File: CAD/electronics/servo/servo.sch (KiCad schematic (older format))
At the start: 16 parts, among them J1 Front ultrasound, J10 Servo7, J11 Start trigger, J2 Rear ultrasound, J3 Servo0, J4 Servo2, J5 Servo4, J6 Servo6, J7 Servo1, J8 Servo3, J9 Servo5, U1 PCF8574

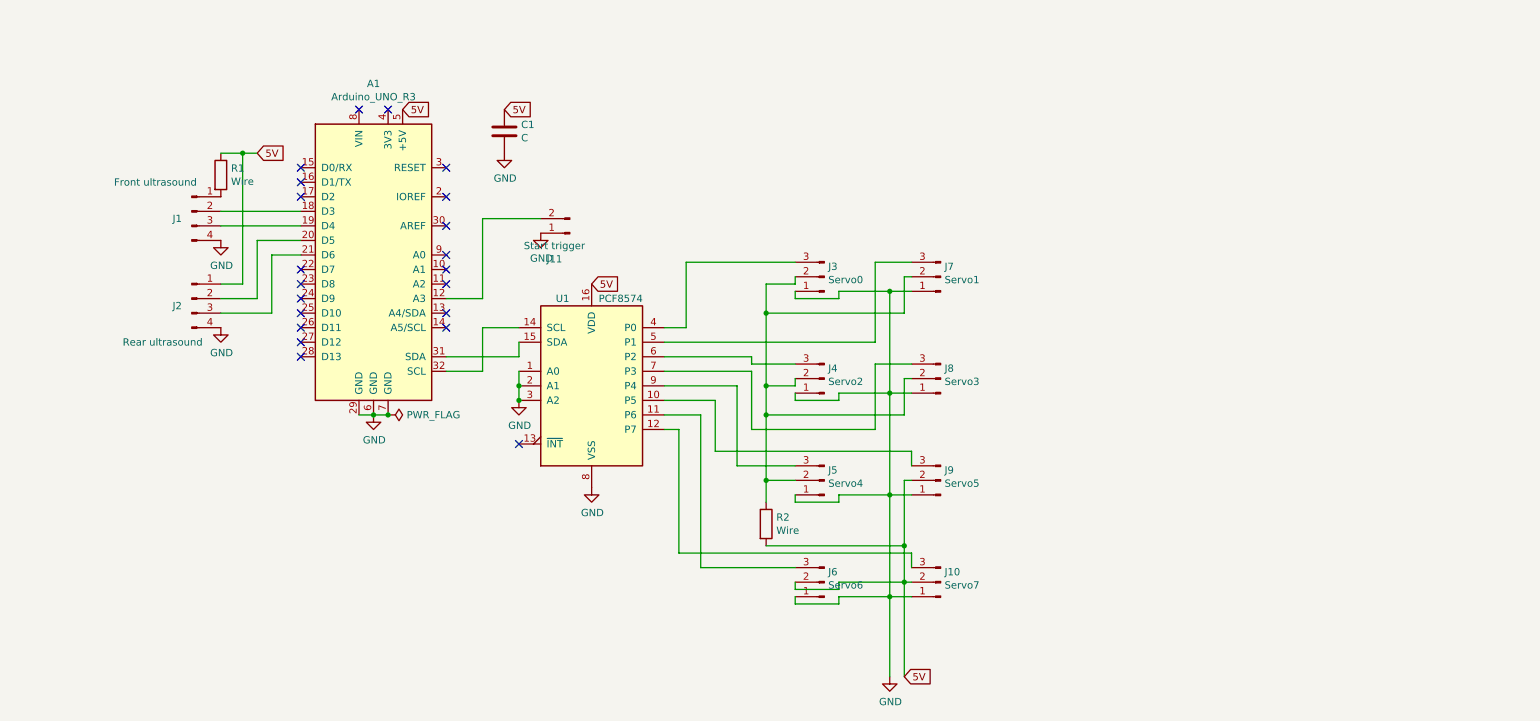
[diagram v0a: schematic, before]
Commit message: Add servo board CAD design.
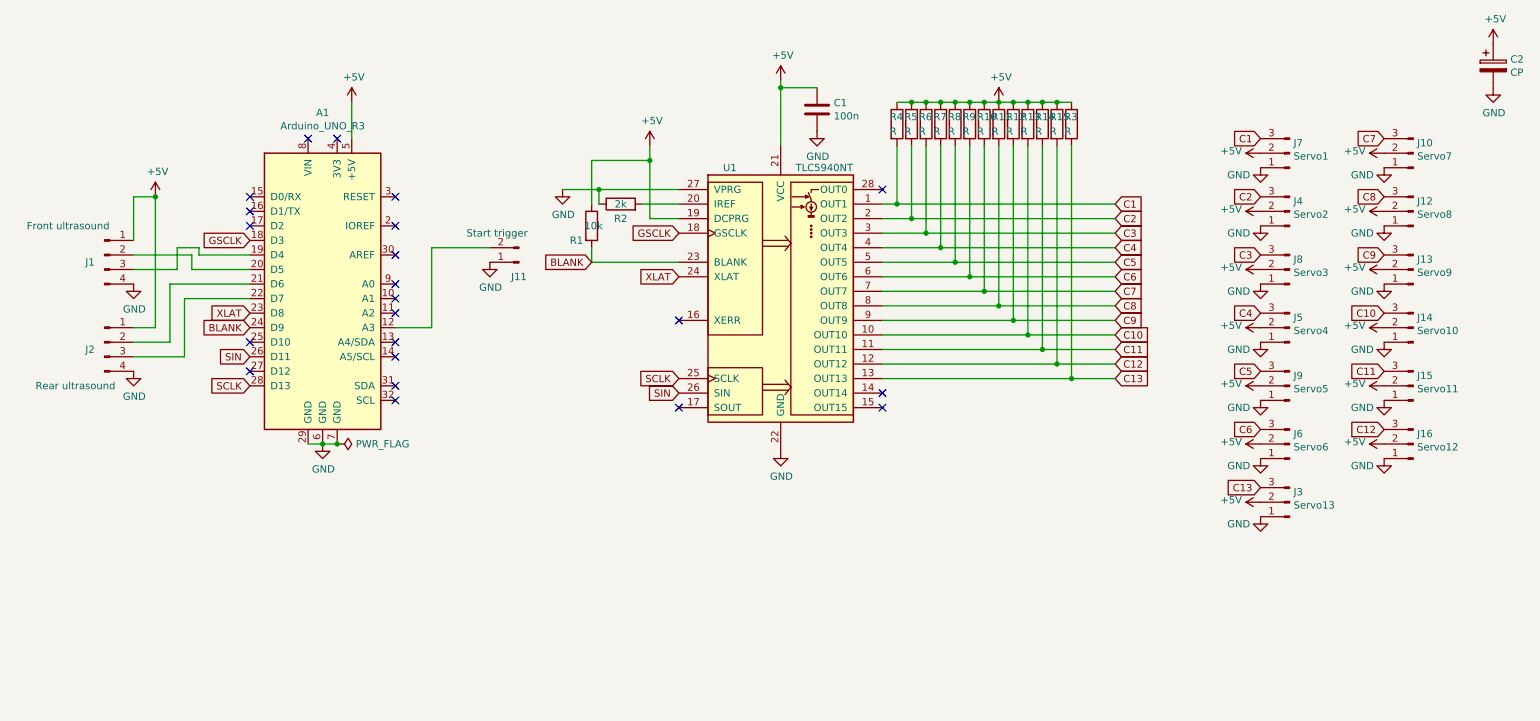
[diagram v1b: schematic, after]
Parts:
- removed U1: PCF8574, Package_DIP:DIP-16_W7.62mm, symbol Interface_Expansion:PCF8574
- added C2: CP, Capacitor_THT:CP_Radial_D8.0mm_P5.00mm, symbol Device:CP
- added J12: Servo8, Connector_PinHeader_2.54mm:PinHeader_1x03_P2.54mm_Vertical, symbol Connector:Conn_01x03_Male
- added J13: Servo9, Connector_PinHeader_2.54mm:PinHeader_1x03_P2.54mm_Vertical, symbol Connector:Conn_01x03_Male
- added J14: Servo10, Connector_PinHeader_2.54mm:PinHeader_1x03_P2.54mm_Vertical, symbol Connector:Conn_01x03_Male
- added J15: Servo11, Connector_PinHeader_2.54mm:PinHeader_1x03_P2.54mm_Vertical, symbol Connector:Conn_01x03_Male
- added J16: Servo12, Connector_PinHeader_2.54mm:PinHeader_1x03_P2.54mm_Vertical, symbol Connector:Conn_01x03_Male
- added R10, R11, R12, R13, R14, R15, R3, R4, R5, R6, R7, R8, R9: R, Resistor_THT:R_Axial_DIN0204_L3.6mm_D1.6mm_P2.54mm_Vertical, symbol Device:R
- added U1: TLC5940NT, Package_DIP:DIP-28_W7.62mm, symbol Driver_LED:TLC5940NT
- C1: value C -> 100n; footprint Capacitor_THT:C_Disc_D5.0mm_W2.5mm_P5.00mm -> Capacitor_THT:C_Disc_D5.1mm_W3.2mm_P5.00mm
- J10, J4, J5, J6, J7, J8, J9: footprint Connector_PinHeader_2.54mm:PinHeader_1x03_P2.54mm_Horizontal -> Connector_PinHeader_2.54mm:PinHeader_1x03_P2.54mm_Vertical
- J3: value Servo0 -> Servo13; footprint Connector_PinHeader_2.54mm:PinHeader_1x03_P2.54mm_Horizontal -> Connector_PinHeader_2.54mm:PinHeader_1x03_P2.54mm_Vertical
- R1: value Wire -> 10k; footprint Resistor_THT:R_Axial_DIN0207_L6.3mm_D2.5mm_P10.16mm_Horizontal -> Resistor_THT:R_Axial_DIN0207_L6.3mm_D2.5mm_P7.62mm_Horizontal
- R2: value Wire -> 2k; footprint Resistor_THT:R_Axial_DIN0207_L6.3mm_D2.5mm_P5.08mm_Vertical -> Resistor_THT:R_Axial_DIN0207_L6.3mm_D2.5mm_P7.62mm_Horizontal
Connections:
- net GND: now also R2.1, C2.2, J12.1 (Pin_1), J13.1 (Pin_1), J14.1 (Pin_1), J15.1 (Pin_1), J16.1 (Pin_1), U1.22 (GND), U1.27 (VPRG)
- net C5: now reaches J9.3 (Pin_3)
- net C5: now also R8.2, U1.5 (OUT5)
- net C6: now reaches J6.3 (Pin_3)
- net C6: now also R9.2, U1.6 (OUT6)
- net C7: now reaches J10.3 (Pin_3)
- net C7: now also R10.2, U1.7 (OUT7)
- net C13: now reaches J3.3 (Pin_3)
- net C13: now also R3.2, U1.13 (OUT13)
- net C1: now reaches J7.3 (Pin_3)
- net C1: now also R4.2, U1.1 (OUT1)
- net C2: now reaches J4.3 (Pin_3)
- net C2: now also R5.2, U1.2 (OUT2)
- net C3: now reaches J8.3 (Pin_3)
- net C3: now also R6.2, U1.3 (OUT3)
- net C4: now reaches J5.3 (Pin_3)
- net C4: now also R7.2, U1.4 (OUT4)
- net at J1.2 (Pin_2): now also A1.20 (D5); no longer A1.18 (D3)
- net at J2.2 (Pin_2): now also A1.21 (D6); no longer A1.20 (D5)
- net at J2.3 (Pin_3): now also A1.22 (D7); no longer A1.21 (D6)
- net XLAT: now reaches A1.23 (D8)
- net XLAT: now also U1.24 (XLAT)
- net BLANK: now reaches A1.24 (D9)
- net BLANK: now also R1.2, U1.23 (BLANK)
- net SIN: now reaches A1.26 (D11)
- net SIN: now also U1.26 (SIN)
- net SCLK: now reaches A1.28 (D13)
- net SCLK: now also U1.25 (SCLK)
- net +5V: now reaches J3.2 (Pin_2), J4.2 (Pin_2), J5.2 (Pin_2), J7.2 (Pin_2), J8.2 (Pin_2)
- net +5V: now also A1.5 (+5V), C1.1, J1.1 (Pin_1), J10.2 (Pin_2), J2.1 (Pin_1), J6.2 (Pin_2), J9.2 (Pin_2), R1.1, C2.1, J12.2 (Pin_2), J13.2 (Pin_2), J14.2 (Pin_2), J15.2 (Pin_2), J16.2 (Pin_2), R10.1, R11.1, R12.1, R13.1, R14.1, R15.1, R3.1, R4.1, R5.1, R6.1, R7.1, R8.1, R9.1, U1.19 (DCPRG), U1.21 (VCC); no longer R2.1
- removed net 5V: A1.5 (+5V), C1.1, J10.2 (Pin_2), J2.1 (Pin_1), J6.2 (Pin_2), J9.2 (Pin_2), R1.1, R2.2
- new net: R2.2, U1.20 (IREF)
- new net C10: J14.3 (Pin_3), R13.2, U1.10 (OUT10)
- new net C11: J15.3 (Pin_3), R14.2, U1.11 (OUT11)
- new net C12: J16.3 (Pin_3), R15.2, U1.12 (OUT12)
- new net C8: J12.3 (Pin_3), R11.2, U1.8 (OUT8)
- new net C9: J13.3 (Pin_3), R12.2, U1.9 (OUT9)
- new net GSCLK: A1.18 (D3), U1.18 (GSCLK)
- no-connect marks 21 -> 22
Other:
- moved on the sheet: A1, J1, J10, J11, J2, J4, J5, J6, J7, J8, J9

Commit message: Nouveau design de carte servo
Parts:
- removed J14: Servo10, Connector_PinHeader_2.54mm:PinHeader_1x03_P2.54mm_Vertical, symbol Connector:Conn_01x03_Male
- removed J15: Servo11, Connector_PinHeader_2.54mm:PinHeader_1x03_P2.54mm_Vertical, symbol Connector:Conn_01x03_Male
- removed J16: Servo12, Connector_PinHeader_2.54mm:PinHeader_1x03_P2.54mm_Vertical, symbol Connector:Conn_01x03_Male
- removed J3: Servo13, Connector_PinHeader_2.54mm:PinHeader_1x03_P2.54mm_Vertical, symbol Connector:Conn_01x03_Male
- removed R15: R, Resistor_THT:R_Axial_DIN0204_L3.6mm_D1.6mm_P2.54mm_Vertical, symbol Device:R
- added J14: GPIO A1, Connector_Molex:Molex_KK-254_AE-6410-02A_1x02_P2.54mm_Vertical, symbol Connector:Conn_01x02_Male
- added J15: GPIO A3, Connector_Molex:Molex_KK-254_AE-6410-02A_1x02_P2.54mm_Vertical, symbol Connector:Conn_01x02_Male
- added J16, J21: I2C, Connector_Molex:Molex_KK-254_AE-6410-04A_1x04_P2.54mm_Vertical, symbol Connector:Conn_01x04_Male
- added J17: Servo power in, Connector_PinSocket_2.54mm:PinSocket_1x02_P2.54mm_Vertical, symbol Connector:Conn_01x02_Male
- added J18: Servo10, Connector_Molex:Molex_KK-254_AE-6410-03A_1x03_P2.54mm_Vertical, symbol Connector:Conn_01x03_Male
- added J19: Servo11, Connector_Molex:Molex_KK-254_AE-6410-03A_1x03_P2.54mm_Vertical, symbol Connector:Conn_01x03_Male
- added J20: Servo12, Connector_Molex:Molex_KK-254_AE-6410-03A_1x03_P2.54mm_Vertical, symbol Connector:Conn_01x03_Male
- added J3: GPIO A2, Connector_Molex:Molex_KK-254_AE-6410-02A_1x02_P2.54mm_Vertical, symbol Connector:Conn_01x02_Male
- A1: symbol MCU_Module:Arduino_UNO_R3 -> servo-rescue:Arduino_UNO_R3-MCU_Module
- C1: footprint Capacitor_THT:C_Disc_D5.1mm_W3.2mm_P5.00mm -> Capacitor_THT:C_Disc_D7.5mm_W5.0mm_P10.00mm
- J1, J2: footprint Connector_PinHeader_2.54mm:PinHeader_1x04_P2.54mm_Horizontal -> Connector_Molex:Molex_KK-254_AE-6410-04A_1x04_P2.54mm_Vertical
- J10, J12, J13, J4, J5, J6, J7, J8, J9: footprint Connector_PinHeader_2.54mm:PinHeader_1x03_P2.54mm_Vertical -> Connector_Molex:Molex_KK-254_AE-6410-03A_1x03_P2.54mm_Vertical
- J11: value Start trigger -> GPIO A0; footprint Connector_PinHeader_2.54mm:PinHeader_1x02_P2.54mm_Horizontal -> Connector_Molex:Molex_KK-254_AE-6410-02A_1x02_P2.54mm_Vertical
- R10, R11, R12, R13, R14, R3, R4, R5, R6, R7, R8, R9: footprint Resistor_THT:R_Axial_DIN0204_L3.6mm_D1.6mm_P2.54mm_Vertical -> Resistor_THT:R_Axial_DIN0204_L3.6mm_D1.6mm_P7.62mm_Horizontal
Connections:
- net +5V: now also J16.4 (Pin_4), J21.4 (Pin_4); no longer C2.1, J10.2 (Pin_2), J12.2 (Pin_2), J13.2 (Pin_2), J4.2 (Pin_2), J5.2 (Pin_2), J6.2 (Pin_2), J7.2 (Pin_2), J8.2 (Pin_2), J9.2 (Pin_2)
- net GND: now also J14.1 (Pin_1), J15.1 (Pin_1), J16.1 (Pin_1), J17.1 (Pin_1), J18.1 (Pin_1), J19.1 (Pin_1), J20.1 (Pin_1), J21.1 (Pin_1), J3.1 (Pin_1)
- net ARDUINO_A1: now reaches A1.10 (A1)
- net ARDUINO_A1: now also J14.2 (Pin_2)
- net ARDUINO_A2: now reaches A1.11 (A2)
- net ARDUINO_A2: now also J3.2 (Pin_2)
- net ARDUINO_A0: now reaches J11.2 (Pin_2)
- net ARDUINO_A0: now also A1.9 (A0); no longer A1.12 (A3)
- net SDA: now reaches A1.13 (A4/SDA)
- net SDA: now also J16.3 (Pin_3), J21.3 (Pin_3)
- net SCL: now reaches A1.14 (A5/SCL)
- net SCL: now also J16.2 (Pin_2), J21.2 (Pin_2)
- net C10 renamed CA
- net CA: now also R3.2, J18.3 (Pin_3); no longer R13.2
- net C11 renamed CB
- net CB: now also R13.2, J19.3 (Pin_3); no longer R14.2
- net C12 renamed CC
- net CC: now also R14.2, J20.3 (Pin_3)
- net C13: no longer names the net of U1.13 (OUT13)
- net C13: no longer R3.2
- new net 5V_SERVO: C2.1, J10.2 (Pin_2), J12.2 (Pin_2), J13.2 (Pin_2), J17.2 (Pin_2), J18.2 (Pin_2), J19.2 (Pin_2), J20.2 (Pin_2), J4.2 (Pin_2), J5.2 (Pin_2), J6.2 (Pin_2), J7.2 (Pin_2), J8.2 (Pin_2), J9.2 (Pin_2)
- new net ARDUINO_A3: A1.12 (A3), J15.2 (Pin_2)
- no-connect marks 22 -> 18
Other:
- moved on the sheet: J10, J11, J12, J13
